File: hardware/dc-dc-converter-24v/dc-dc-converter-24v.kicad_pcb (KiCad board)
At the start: 2 copper layers, 100 x 100 mm, 49 parts, among them IC1 LM5122MHX_NOPB, J1 12V, J2 24V, Q1 SQJA42EP, Q2 SQJA42EP

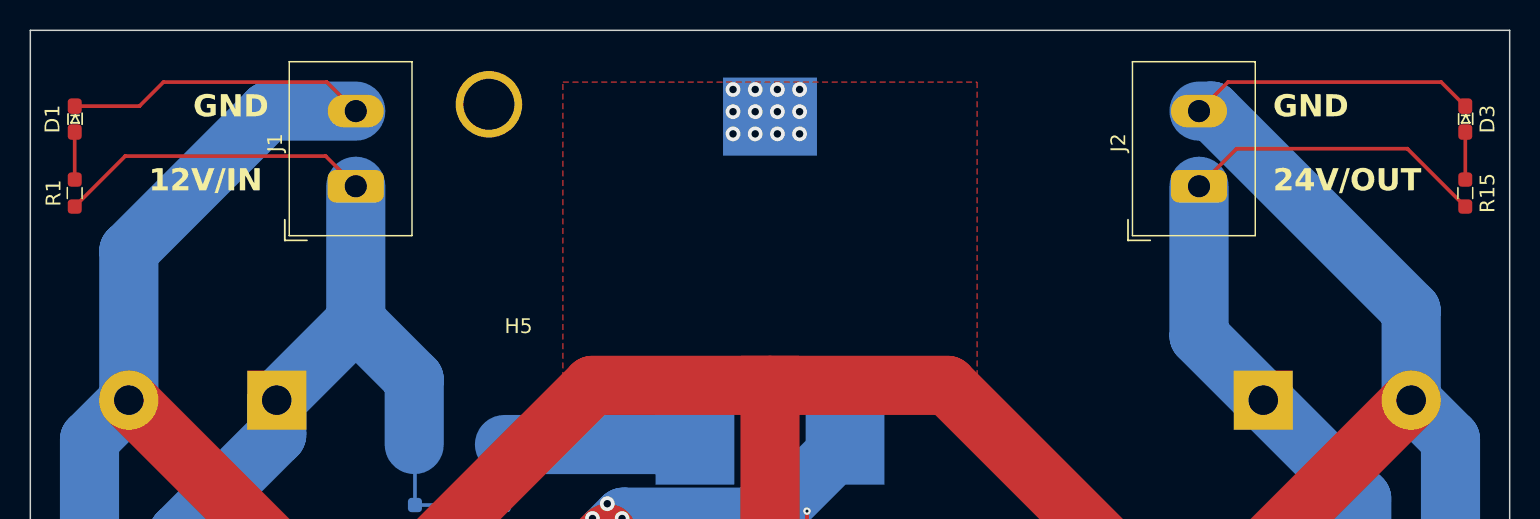
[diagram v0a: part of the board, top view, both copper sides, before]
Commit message: flip connectors to bottom
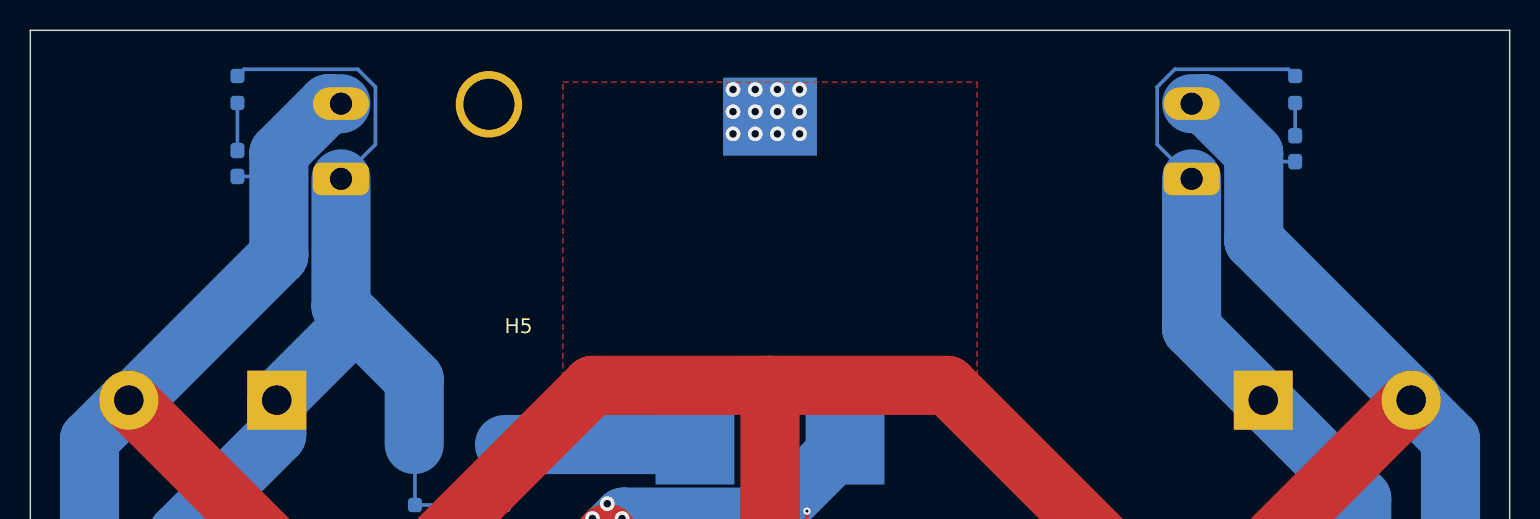
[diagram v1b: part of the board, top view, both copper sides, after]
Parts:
- D1, D3, J1, J2, R1, R15: moved to B.Cu
- moved R15 13.5 mm to (105.5, 24.0), turned to -90 degrees
- moved R1 13.0 mm to (34.0, 24.0), turned to -90 degrees
- moved D3 11.7 mm to (105.5, 28.0), turned to 90 degrees
- moved D1 11.4 mm to (34.0, 29.0), turned to 90 degrees
- moved J1 1.12 mm to (41.0, 27.5)
- moved J2 0.71 mm to (98.5, 27.5)
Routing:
- net GND: track 411.5 -> 376.1 mm
- net /Vin: track 102.4 -> 99.3 mm
- net /Vout: track 169.5 -> 166.7 mm
- net Net-(D3-A): track 3.21 -> 2.21 mm

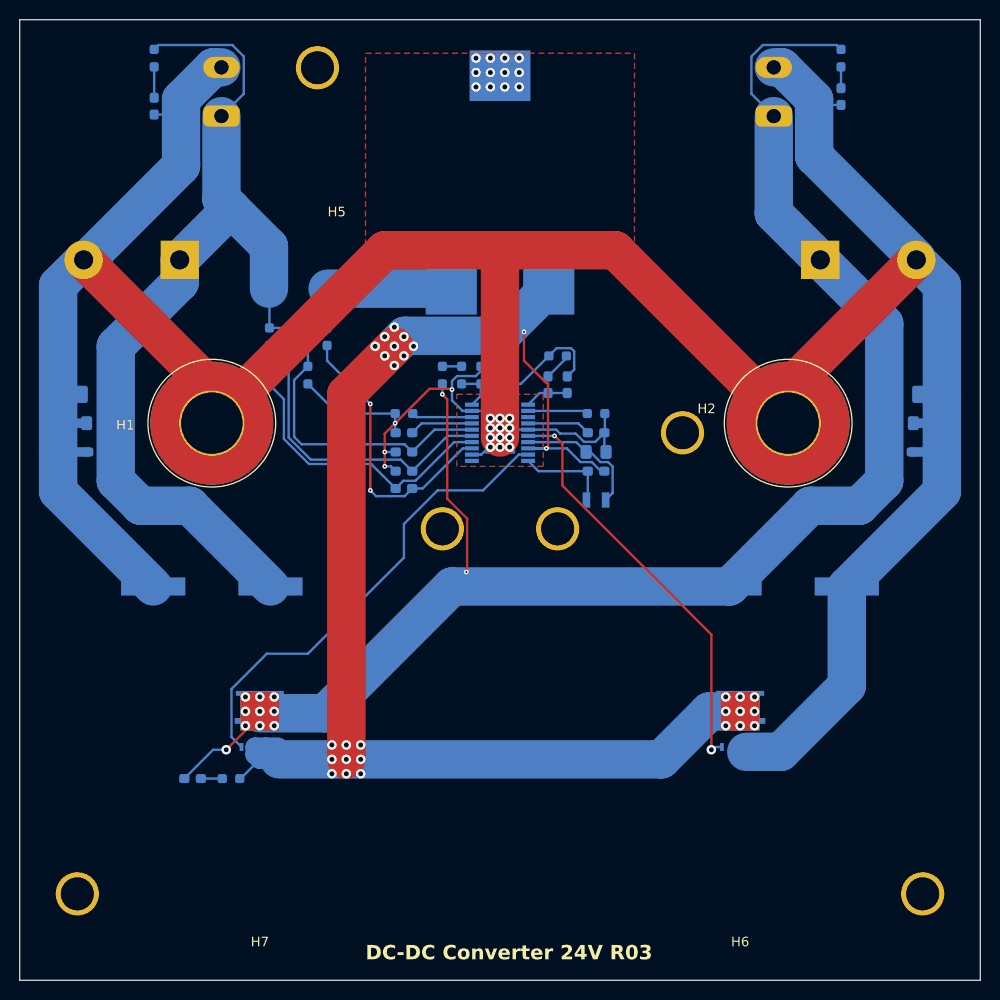
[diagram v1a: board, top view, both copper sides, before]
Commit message: change type of heatsinks
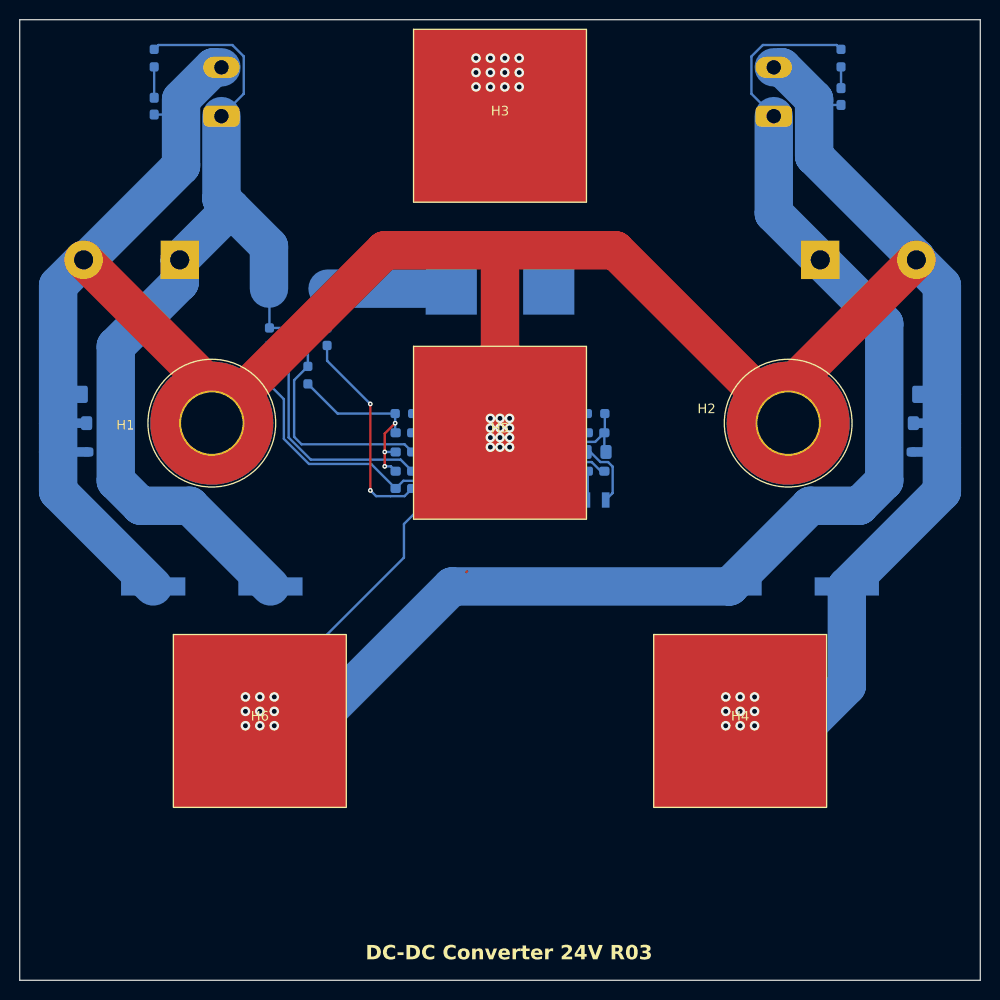
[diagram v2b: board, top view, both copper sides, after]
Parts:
- removed H7: heatsink_HSB43-454515P, benediktibk:HSB43-454515P
- added H3: ~, benediktibk:heatsink_18x18, F.Cu at (70.0, 30.0)
- added H4: ~, benediktibk:heatsink_18x18, F.Cu at (95.0, 93.0)
- H5, H6: value heatsink_HSB43-454515P -> ~; footprint benediktibk:HSB43-454515P -> benediktibk:heatsink_18x18
- moved H6 50.0 mm to (45.0, 93.0), turned to 0 degrees
- moved H5 19.0 mm to (70.0, 63.0), turned to 0 degrees
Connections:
- H6 pad PAD: Net-(IC1-SW) -> /Vout
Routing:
- net Net-(IC1-SW): track 146.7 -> 10.9 mm, vias 29 -> 9
- net Net-(IC1-LO): track 43.4 -> 2.75 mm, vias 2 -> 0
- net /Vout: track 166.7 -> 135.5 mm, vias 12 -> 9
- net GND: track 376.1 -> 368.9 mm, vias 28 -> 27
- removed copper zone on F.Cu, net GND

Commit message: finish layout for dc-dc converter
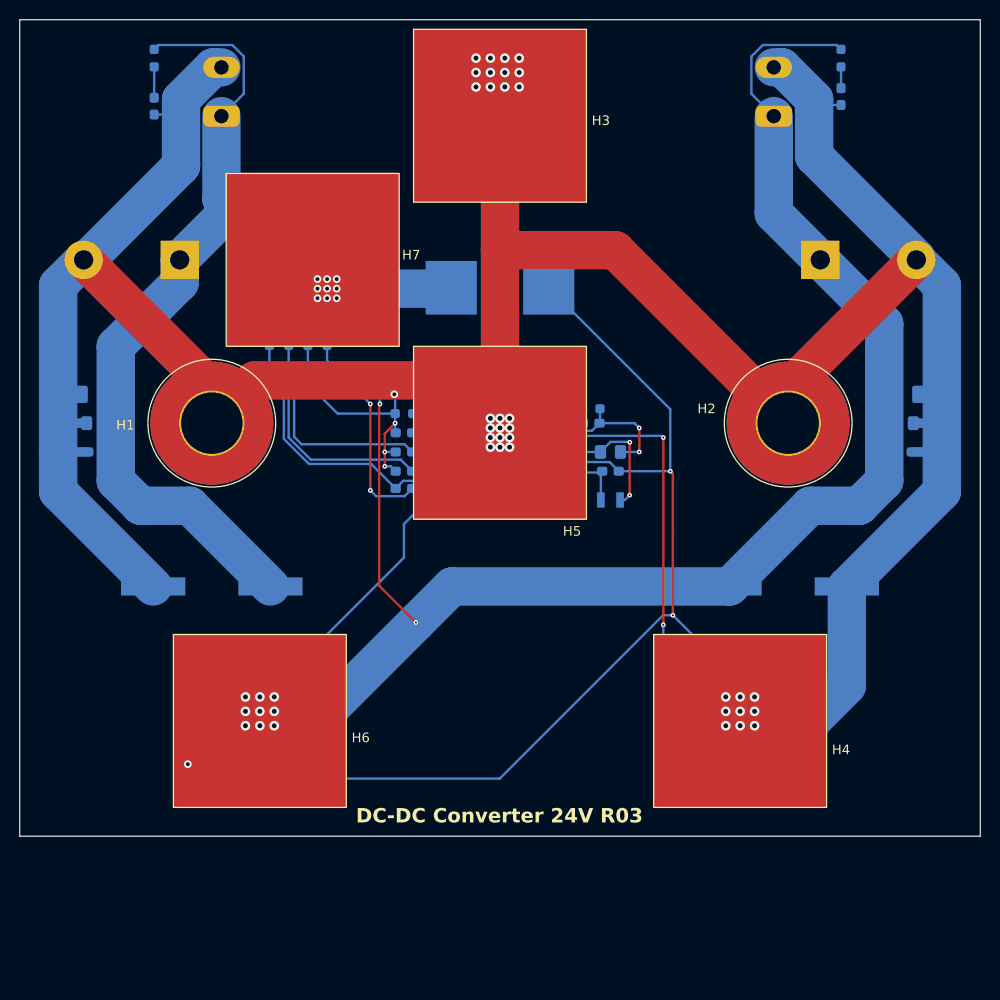
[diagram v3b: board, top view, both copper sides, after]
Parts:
- added H7: ~, benediktibk:heatsink_18x18, F.Cu at (50.5, 45.0)
- moved C12 1.50 mm to (81.5, 67.0)
- moved C14 1.50 mm to (81.5, 65.0)
- moved D2 1.50 mm to (81.5, 70.0)
- moved C13 1.12 mm to (79.5, 62.0)
- moved R13 0.71 mm to (79.5, 60.5)
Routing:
- net Net-(IC1-SW): track 10.9 -> 124.6 mm, vias 9 -> 11
- net Net-(IC1-LO): track 2.75 -> 48.9 mm, vias 0 -> 2
- net /Vout: track 135.5 -> 169.1 mm, vias 9 -> 12
- net GND: track 368.9 -> 377.6 mm, vias 27 -> 30
- net Net-(D2-A): track 13.6 -> 18.2 mm, vias 0 -> 2
- net Net-(D2-K): track 9.71 -> 11.1 mm
- net Net-(IC1-RES): track 6.62 -> 5.24 mm
- net Net-(IC1-SLOPE): track 6.28 -> 5.76 mm
- net Net-(H7-PadPAD): vias 0 -> 9
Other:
- board size 100 x 100 mm -> 100 x 85 mm

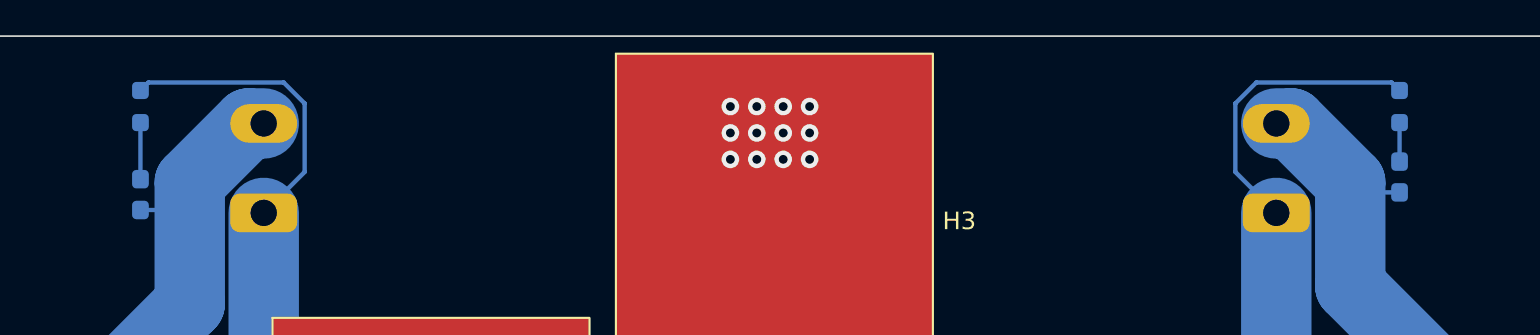
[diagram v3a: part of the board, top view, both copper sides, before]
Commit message: update symbols and footprints
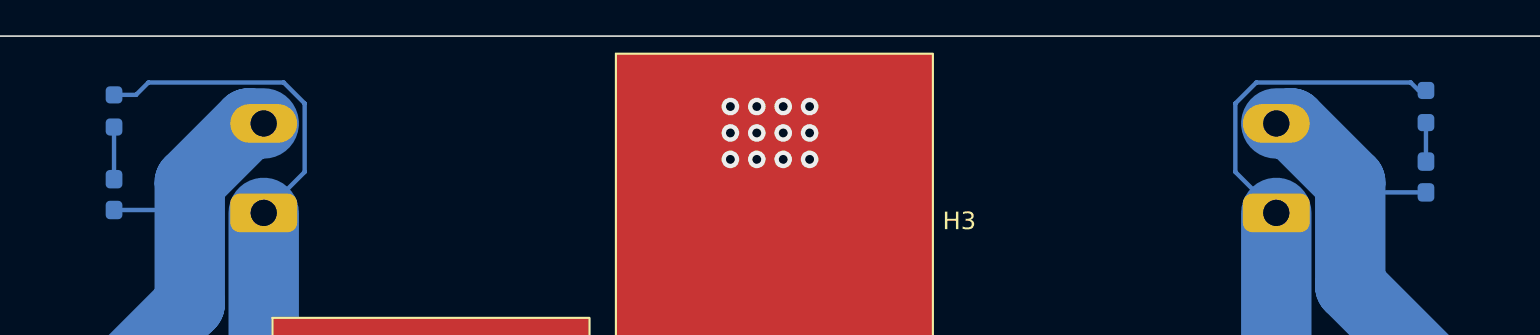
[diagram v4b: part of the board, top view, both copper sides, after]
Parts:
- moved R1 1.52 mm to (32.5, 24.2)
- moved D1 1.50 mm to (32.5, 29.0)
- moved D3 1.50 mm to (107.0, 28.0)
- moved R15 1.50 mm to (107.0, 24.0)
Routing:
- net GND: track 377.6 -> 380.6 mm
- net /Vin: track 99.3 -> 100.9 mm
- net /Vout: track 169.1 -> 170.6 mm
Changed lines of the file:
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@@
 	(footprint "benediktibk:D_0603_1608Metric_Pad1.05x0.95mm_HandSolder"
 		(layer "B.Cu")
-		(at 34 29 90)
+		(at 32.5 29 90)
 		(descr "Diode SMD 0603 (1608 Metric), square (rectangular) end terminal, IPC_7351 nominal, (Body size source: http://www.tortai-tech.com/upload/download/2011102023233369053.pdf), generated with kicad-footprint-generator")
 		(tags "diode handsolder")
 		(property "Reference" "D1"
-			(at 0 -1.5 90)
+			(at -2.75 0 180)
 			(layer "B.SilkS")
 			(effects
@@
 	(footprint "benediktibk:R_0603_1608Metric_Pad0.98x0.95mm_HandSolder"
 		(layer "B.Cu")
-		(at 105.5 24 -90)
+		(at 107 24 -90)
 		(descr "Resistor SMD 0603 (1608 Metric), square (rectangular) end terminal, IPC_7351 nominal with elongated pad for handsoldering. (Body size source: IPC-SM-782 page 72, https://www.pcb-3d.com/wordpress/wp-content/uploads/ipc-sm-782a_amendment_1_and_2.pdf), generated with kicad-footprint-generator")
 		(tags "resistor handsolder")
 		(property "Reference" "R15"
-			(at 0 -1.5 90)
+			(at -2.5 -0.25 0)
 			(layer "B.SilkS")
 			(effects
@@
 	(footprint "benediktibk:R_0603_1608Metric_Pad0.98x0.95mm_HandSolder"
 		(layer "B.Cu")
-		(at 34 24 -90)
+		(at 32.5 24.25 -90)
 		(descr "Resistor SMD 0603 (1608 Metric), square (rectangular) end terminal, IPC_7351 nominal with elongated pad for handsoldering. (Body size source: IPC-SM-782 page 72, https://www.pcb-3d.com/wordpress/wp-content/uploads/ipc-sm-782a_amendment_1_and_2.pdf), generated with kicad-footprint-generator")
 		(tags "resistor handsolder")
 		(property "Reference" "R1"
-			(at 0 1.43 90)
+			(at -2.5 0 180)
 			(layer "B.SilkS")
 			(effects
@@
 			(layer "B.SilkS")
 		)
-		(fp_line
-			(start 6.2 -4)
-			(end -6.4 -4)
-			(stroke
-				(width 0.05)
-				(type default)
-			)
-			(layer "B.CrtYd")
-		)
-		(fp_line
-			(start -6.4 -4)
-			(end -6.4 5)
-			(stroke
-				(width 0.05)
-				(type default)
-			)
-			(layer "B.CrtYd")
-		)
-		(fp_line
-			(start 6.2 5)
-			(end 6.2 -4)
-			(stroke
-				(width 0.05)
-				(type default)
-			)
-			(layer "B.CrtYd")
-		)
-		(fp_line
-			(start -6.4 5)
-			(end 6.2 5)
+		(fp_rect
+			(start -6.5 7)
+			(end 6.5 -6)
 			(stroke
 				(width 0.05)
 				(type default)
 			)
+			(fill none)
 			(layer "B.CrtYd")
 		)
@@
 	(footprint "benediktibk:D_0603_1608Metric_Pad1.05x0.95mm_HandSolder"
 		(layer "B.Cu")
-		(at 105.5 28 90)
+		(at 107 28 90)
 		(descr "Diode SMD 0603 (1608 Metric), square (rectangular) end terminal, IPC_7351 nominal, (Body size source: http://www.tortai-tech.com/upload/download/2011102023233369053.pdf), generated with kicad-footprint-generator")
 		(tags "diode handsolder")
 		(property "Reference" "D3"
-			(at 0 1.5 90)
+			(at -2.75 0 180)
 			(layer "B.SilkS")
 			(effects
@@
 			(layer "B.SilkS")
 		)
-		(fp_line
-			(start 6.2 -4)
-			(end -6.4 -4)
-			(stroke
-				(width 0.05)
-				(type default)
-			)
-			(layer "B.CrtYd")
-		)
-		(fp_line
-			(start -6.4 -4)
-			(end -6.4 5)
-			(stroke
-				(width 0.05)
-				(type default)
-			)
-			(layer "B.CrtYd")
-		)
-		(fp_line
-			(start 6.2 5)
-			(end 6.2 -4)
-			(stroke
-				(width 0.05)
-				(type default)
-			)
-			(layer "B.CrtYd")
-		)
-		(fp_line
-			(start -6.4 5)
-			(end 6.2 5)
+		(fp_rect
+			(start -6.5 7)
+			(end 6.5 -6)
 			(stroke
 				(width 0.05)
 				(type default)
 			)
+			(fill none)
 			(layer "B.CrtYd")
 		)
@@
 	)
 	(gr_text "GND"
-		(at 112.5 25.5 -0)
+		(at 114 26 -0)
 		(layer "B.SilkS")
 		(effects
@@
 	)
 	(gr_text "12V/IN"
-		(at 116 31 -0)
+		(at 117.5 31.5 -0)
 		(layer "B.SilkS")
 		(effects
@@
 	)
 	(segment
+		(start 107 28.875)
+		(end 103.274697 28.875)
+		(width 0.25)
+		(layer "B.Cu")
+		(net 2)
+	)
+	(segment
 		(start 27 45)
 		(end 36.8 35.2)
@@
 	)
 	(segment
-		(start 105.5 28.875)
-		(end 103.274697 28.875)
-		(width 0.25)
-		(layer "B.Cu")
-		(net 2)
-	)
-	(segment
 		(start 65 59.625)
 		(end 66.1 60.725)
@@
 	)
 	(segment
-		(start 103.274697 28.875)
-		(end 102.7 28.300303)
-		(width 0.25)
-		(layer "B.Cu")
-		(net 2)
-	)
-	(segment
 		(start 72.925 62.675)
 		(end 75.838173 62.675)
@@
 	)
 	(segment
+		(start 35.225303 29.875)
+		(end 32.5 29.875)
+		(width 0.25)
+		(layer "B.Cu")
+		(net 2)
+	)
+	(segment
 		(start 75.838173 62.675)
 		(end 75.963173 62.8)
@@
 	)
 	(segment
+		(start 103.274697 28.875)
+		(end 102.7 28.300303)
+		(width 0.25)
+		(layer "B.Cu")
+		(net 2)
+	)
+	(segment
 		(start 40.140303 24.96)
 		(end 41 24.96)
@@
 	)
 	(segment
-		(start 35.225303 29.875)
-		(end 36.8 28.300303)
-		(width 0.25)
-		(layer "B.Cu")
-		(net 2)
-	)
-	(segment
 		(start 116 69.103101)
 		(end 116 64.5)
@@
 	)
 	(segment
-		(start 34 29.875)
+		(start 36.8 28.300303)
 		(end 35.225303 29.875)
 		(width 0.25)
@@
 	)
 	(segment
-		(start 96.175 27.715)
-		(end 98.5 30.04)
-		(width 0.25)
+		(start 51.801 92.199)
+		(end 45 92.199)
+		(width 4)
 		(layer "B.Cu")
 		(net 5)
 	)
 	(segment
-		(start 51.801 92.199)
-		(end 45 92.199)
+		(start 65 79)
+		(end 61.25 82.75)
 		(width 4)
 		(layer "B.Cu")
@@
 	)
 	(segment
-		(start 97.365 22.635)
-		(end 96.175 23.825)
-		(width 0.25)
+		(start 107.4 70.6)
+		(end 102.296899 70.6)
+		(width 4)
 		(layer "B.Cu")
 		(net 5)
 	)
 	(segment
-		(start 96.175 23.825)
-		(end 96.175 27.715)
-		(width 0.25)
+		(start 110 68)
+		(end 107.4 70.6)
+		(width 4)
 		(layer "B.Cu")
 		(net 5)
 	)
 	(segment
-		(start 65 79)
-		(end 61.25 82.75)
-		(width 4)
+		(start 106.135 22.635)
+		(end 106.5875 23.0875)
+		(width 0.25)
 		(layer "B.Cu")
 		(net 5)
 	)
 	(segment
-		(start 107.4 70.6)
-		(end 102.296899 70.6)
-		(width 4)
+		(start 97.365 22.635)
+		(end 106.135 22.635)
+		(width 0.25)
 		(layer "B.Cu")
 		(net 5)
 	)
 	(segment
-		(start 110 68)
-		(end 107.4 70.6)
-		(width 4)
+		(start 96.175 23.825)
+		(end 97.365 22.635)
+		(width 0.25)
 		(layer "B.Cu")
 		(net 5)
@@
 	)
 	(segment
-		(start 105.0475 22.635)
-		(end 97.365 22.635)
-		(width 0.25)
-		(layer "B.Cu")
-		(net 5)
-	)
-	(segment
 		(start 103.342169 45)
 		(end 98.5 40.157831)
@@
 	)
 	(segment
-		(start 61.25 82.75)
-		(end 51.801 92.199)
-		(width 4)
+		(start 98.5 30.04)
+		(end 96.175 27.715)
+		(width 0.25)
 		(layer "B.Cu")
 		(net 5)
 	)
 	(segment
-		(start 105.5 23.0875)
-		(end 105.0475 22.635)
-		(width 0.25)
+		(start 61.25 82.75)
+		(end 51.801 92.199)
+		(width 4)
 		(layer "B.Cu")
 		(net 5)
@@
 	)
 	(segment
+		(start 106.5875 23.0875)
+		(end 107 23.0875)
+		(width 0.25)
+		(layer "B.Cu")
+		(net 5)
+	)
+	(segment
 		(start 37.1375 99)
 		(end 37.1375 97.8625)
@@
 	)
 	(segment
+		(start 96.175 27.715)
+		(end 96.175 23.825)
+		(width 0.25)
+		(layer "B.Cu")
+		(net 5)
+	)
+	(segment
 		(start 56.5 69)
 		(end 56.5 60)
@@
 	)
 	(segment
+		(start 33.75 23.3375)
+		(end 32.5 23.3375)
+		(width 0.25)
+		(layer "B.Cu")
+		(net 14)
+	)
+	(segment
 		(start 42.135 22.635)
 		(end 43.325 23.825)
@@
 	)
 	(segment
-		(start 34 23.0875)
-		(end 34.4525 22.635)
-		(width 0.25)
-		(layer "B.Cu")
-		(net 14)
-	)
-	(segment
 		(start 42 39.657832)
 		(end 36.657832 45)
@@
 	)
 	(segment
+		(start 34.4525 22.635)
+		(end 33.75 23.3375)
+		(width 0.25)
+		(layer "B.Cu")
+		(net 14)
+	)
+	(segment
 		(start 30 54)
 		(end 30 68)
@@
 	)
 	(segment
-		(start 34 24.9125)
-		(end 34 28.125)
+		(start 32.5 28.125)
+		(end 32.5 25.1625)
 		(width 0.25)
 		(layer "B.Cu")
@@
 	)
 	(segment
-		(start 105.5 24.9125)
-		(end 105.5 27.125)
+		(start 107 24.9125)
+		(end 107 27.125)
 		(width 0.25)
 		(layer "B.Cu")
